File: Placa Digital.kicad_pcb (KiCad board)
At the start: 2 copper layers, 60 x 60 mm, 11 parts, among them J1 SALIDAS, J2 HMI, J4 ENTRADAS, U1 ESP32-DEVKITC-32D, U2 Alimentación

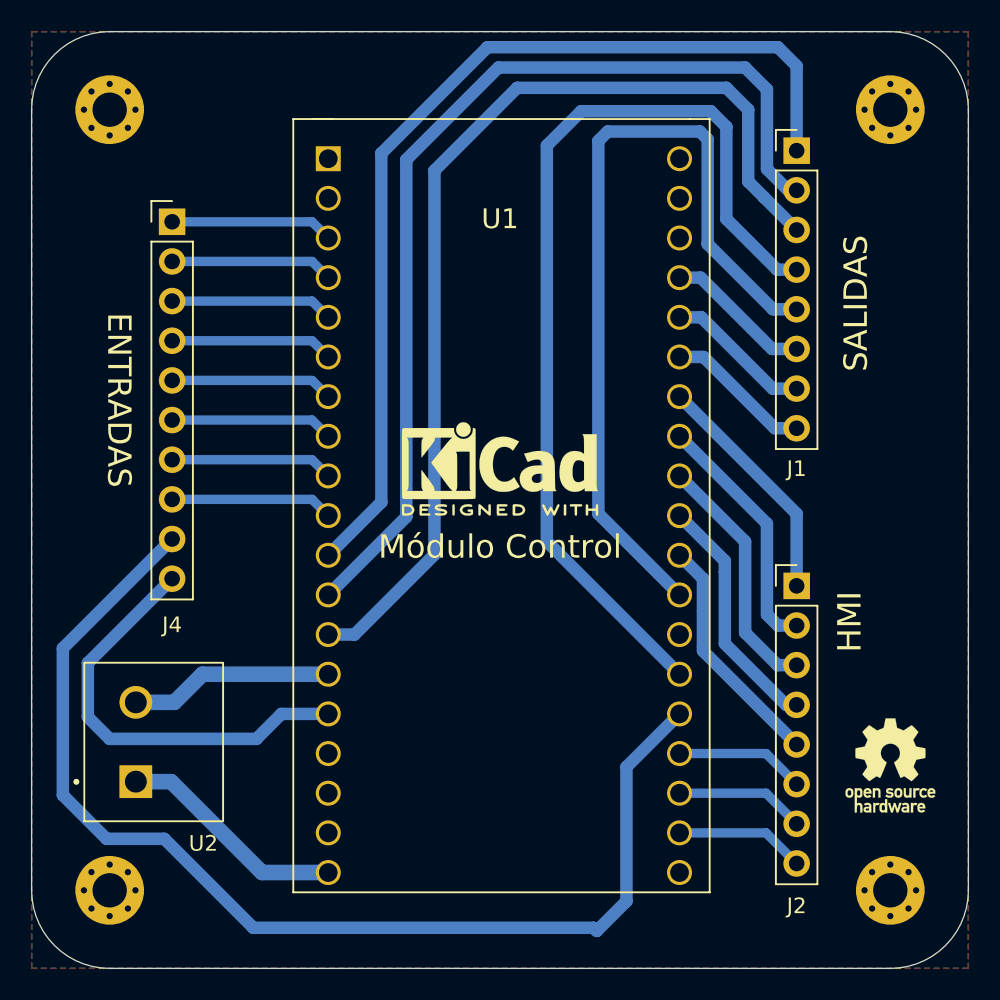
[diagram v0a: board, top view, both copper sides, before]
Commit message: Add 3d model + 1 Layer
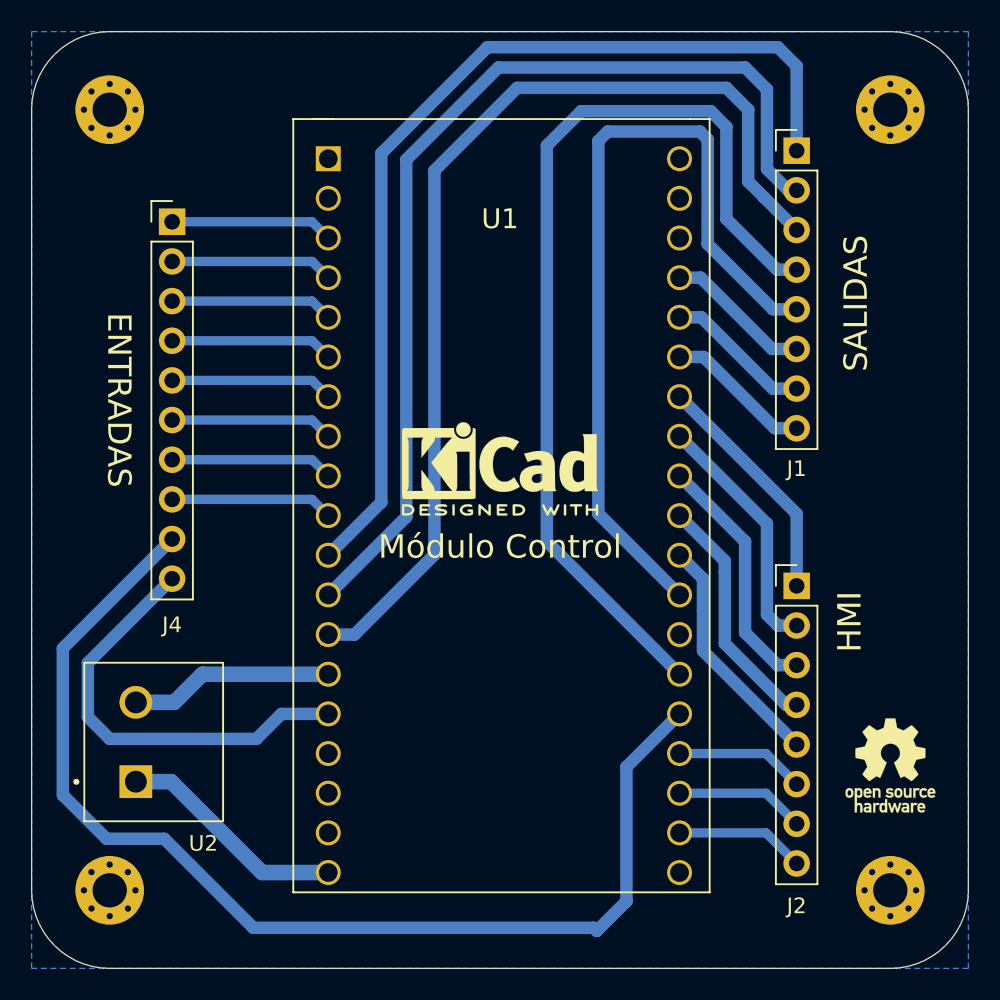
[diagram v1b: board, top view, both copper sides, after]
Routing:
- added copper zone on B.Cu, net GND
- removed copper zone on B.Cu, net /toMicroC_Button3
- removed copper zone on F.Cu, net /toMicroC_Button3
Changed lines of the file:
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@@
     (pad "38" thru_hole circle locked (at 9.5 -22.86) (size 1.6 1.6) (drill 1.2) (layers *.Cu *.Mask)
       (net 16 "unconnected-(U1-Pad38)") (pinfunction "CLK") (pintype "input+no_connect"))
-    (model "ESP32-DevKitC.stp"
-      (offset (xyz 0 0 0))
-      (scale (xyz 1 1 1))
-      (rotate (xyz 0 0 0))
-    )
-    (model "D:/Tesis-Backup-07-08-2021/Kicad/Footprint/ESP32 Development Board/User Library-Goouuu-ESP32 Development Board.STEP"
-      (offset (xyz -2 0 3.5))
+    (model "D:/Tesis-Backup-07-08-2021/Kicad/CEDCp/Modelos_3D_CEDCp/ESP32-DEVKITC-DevBoard.step"
+      (offset (xyz -1.8 0 5))
       (scale (xyz 1 1 1))
       (rotate (xyz -90 0 0))
@@
     (pad "2" thru_hole circle (at 2.54 0 90) (size 2.1 2.1) (drill 1.4) (layers *.Cu *.Mask)
       (net 35 "GND") (pintype "input"))
-    (model "D:/Tesis-Backup-07-08-2021/Kicad/Modelo 3D CEDCp/Bornera_1x2.STEP"
+    (model "D:/Tesis-Backup-07-08-2021/Kicad/CEDCp/Modelos_3D_CEDCp/Bornera_1x2.STEP"
       (offset (xyz 0 -1.2 0))
       (scale (xyz 1 1 1))
-      (rotate (xyz -90 0 180))
+      (rotate (xyz -90 0 -180))
     )
   )
@@
   (segment (start 119.676098 102.04) (end 121.94 102.04) (width 1) (layer "B.Cu") (net 36))
   (segment (start 127.76 107.86) (end 132 107.86) (width 1) (layer "B.Cu") (net 36))
-  (zone (net 8) (net_name "/toMicroC_Button3") (layers F&B.Cu) (hatch edge 0.508)
-    (connect_pads yes (clearance 0.508))
+  (zone (net 35) (net_name "GND") (layer "B.Cu") (hatch edge 0.508)
+    (connect_pads (clearance 0.508))
     (min_thickness 0.254) (filled_areas_thickness no)
     (fill yes (thermal_gap 0.508) (thermal_bridge_width 0.508))

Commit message: Replacement
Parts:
- moved J1 2.69 mm to (163.0, 64.1)
- moved J2 2.69 mm to (163.0, 87.0)
- moved U2 2.00 mm to (121.0, 98.0)
- moved J4 1.04 mm to (122.0, 67.2)
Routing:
- net /fromMicroC_DACI2C_SCL: track 62.0 -> 85.4 mm
- net /toMicroC_ADC_BUSY: track 27.7 -> 14.3 mm
- net GND: track 13.1 -> 0.00 mm
- net /toMicroC_OverVoltageSignal: track 73.2 -> 63.7 mm, vias 0 -> 2
- net /fromMicroC_ADC_CONV: track 65.4 -> 69.3 mm
- net /fromMicroC_ADC_RST: track 63.6 -> 67.4 mm
- net /fromMicroC_DACI2C_SDA: track 52.8 -> 56.0 mm
- net /fromMicroC_ADC_RD: track 62.5 -> 64.9 mm
- net /toMicroC_EncoderButton: track 15.9 -> 13.7 mm
- net /fromMicroC_DisplaySID: track 15.2 -> 13.1 mm
- net /fromMicroC_DisplaySCLK: track 15.9 -> 13.8 mm
- net /fromMicroC_A6841SerialDataIN: track 9.39 -> 11.4 mm
- net /fromMicroC_A6841ST1: track 9.39 -> 11.4 mm
- net /fromMicroC_A6841CLK1: track 9.39 -> 11.4 mm
- net /toMicroC_EncoderSignalB: track 15.6 -> 14.1 mm
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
